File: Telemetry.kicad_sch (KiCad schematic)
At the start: 0 parts

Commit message: idk
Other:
- sheet LeaderSOM4 ports: added none; removed +12V_CarCAN, GND_CarCAN
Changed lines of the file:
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@@
 	(rectangle
 		(start 18.415 18.415)
-		(end 245.745 104.775)
+		(end 229.87 104.775)
 		(stroke
 			(width 0.508)
@@
 	)
 	(bus_entry
-		(at 38.735 60.96)
+		(at 38.1 60.96)
 		(size 2.54 -2.54)
 		(stroke
@@
 	)
 	(bus_entry
-		(at 38.735 57.15)
+		(at 38.1 57.15)
 		(size 2.54 -2.54)
 		(stroke
@@
 	)
 	(bus_entry
-		(at 38.735 53.34)
-		(size 2.54 -2.54)
-		(stroke
-			(width 0)
-			(type default)
-		)
-	)
-	(bus_entry
 		(at 153.035 34.29)
 		(size 2.54 2.54)
@@
 	)
 	(bus_entry
-		(at 38.735 64.77)
-		(size 2.54 -2.54)
-		(stroke
-			(width 0)
-			(type default)
-		)
-	)
-	(bus_entry
 		(at 206.375 30.48)
 		(size 2.54 2.54)
@@
 	(wire
 		(pts
+			(xy 40.64 58.42) (xy 41.91 58.42)
+		)
+		(stroke
+			(width 0)
+			(type default)
+		)
+	)
+	(wire
+		(pts
 			(xy 82.55 54.61) (xy 83.185 54.61)
 		)
@@
 	(bus
 		(pts
-			(xy 38.735 60.96) (xy 38.735 64.77)
-		)
-		(stroke
-			(width 0)
-			(type default)
-		)
-	)
-	(bus
-		(pts
 			(xy 85.725 57.15) (xy 85.725 60.96)
 		)
@@
 		)
 	)
-	(wire
-		(pts
-			(xy 41.275 54.61) (xy 41.91 54.61)
-		)
-		(stroke
-			(width 0)
-			(type default)
-		)
-	)
 	(bus
 		(pts
@@
 	(bus
 		(pts
-			(xy 38.735 57.15) (xy 38.735 60.96)
+			(xy 38.1 57.15) (xy 38.1 60.96)
 		)
 		(stroke
@@
 		(pts
 			(xy 108.585 52.705) (xy 121.285 52.705)
+		)
+		(stroke
+			(width 0)
+			(type default)
+		)
+	)
+	(wire
+		(pts
+			(xy 40.64 54.61) (xy 41.91 54.61)
 		)
 		(stroke
@@
 		)
 	)
+	(bus
+		(pts
+			(xy 38.1 60.96) (xy 38.1 62.23)
+		)
+		(stroke
+			(width 0)
+			(type default)
+		)
+	)
 	(wire
 		(pts
@@
 		(pts
 			(xy 82.55 50.8) (xy 83.185 50.8)
-		)
-		(stroke
-			(width 0)
-			(type default)
-		)
-	)
-	(wire
-		(pts
-			(xy 41.275 58.42) (xy 41.91 58.42)
 		)
 		(stroke
@@
 	(wire
 		(pts
-			(xy 41.275 50.8) (xy 41.91 50.8)
-		)
-		(stroke
-			(width 0)
-			(type default)
-		)
-	)
-	(bus
-		(pts
-			(xy 38.735 53.34) (xy 38.735 57.15)
-		)
-		(stroke
-			(width 0)
-			(type default)
-		)
-	)
-	(wire
-		(pts
-			(xy 41.275 62.23) (xy 41.91 62.23)
-		)
-		(stroke
-			(width 0)
-			(type default)
-		)
-	)
-	(wire
-		(pts
-			(xy 31.75 43.18) (xy 41.91 43.18)
+			(xy 35.56 43.18) (xy 41.91 43.18)
 		)
 		(stroke
@@
 		)
 	)
-	(bus
-		(pts
-			(xy 38.735 64.77) (xy 38.735 67.31)
-		)
-		(stroke
-			(width 0)
-			(type default)
-		)
-	)
 	(wire
 		(pts
@@
 	(wire
 		(pts
-			(xy 31.75 45.72) (xy 41.91 45.72)
+			(xy 35.56 45.72) (xy 41.91 45.72)
 		)
 		(stroke
@@
 		)
 	)
-	(label "12V_Out4"
-		(at 31.75 43.18 0)
-		(effects
-			(font
-				(size 1.27 1.27)
-			)
-			(justify left bottom)
-		)
-	)
 	(label "LTE"
 		(at 30.48 76.2 0)
@@
 	)
 	(label "CarCAN"
-		(at 38.735 61.595 180)
+		(at 38.1 60.96 180)
 		(effects
 			(font
@@
 		)
 	)
-	(label "GND_Out4"
-		(at 31.75 45.72 0)
-		(effects
-			(font
-				(size 1.27 1.27)
-			)
-			(justify left bottom)
-		)
-	)
 	(label "GPS"
 		(at 30.48 69.85 0)
@@
 			)
 			(justify left bottom)
+		)
+	)
+	(hierarchical_label "12V_In"
+		(shape input)
+		(at 35.56 43.18 180)
+		(effects
+			(font
+				(size 1.27 1.27)
+			)
+			(justify right)
+		)
+	)
+	(hierarchical_label "GND_In"
+		(shape input)
+		(at 35.56 45.72 180)
+		(effects
+			(font
+				(size 1.27 1.27)
+			)
+			(justify right)
 		)
 	)
@@
 			)
 		)
-		(pin "GND_CarCAN" input
-			(at 41.91 62.23 180)
-			(effects
-				(font
-					(size 1.27 1.27)
-				)
-				(justify left)
-			)
-		)
 		(pin "+12V_PCAN" output
 			(at 82.55 46.99 0)
@@
 			)
 		)
-		(pin "+12V_CarCAN" input
-			(at 41.91 50.8 180)
-			(effects
-				(font
-					(size 1.27 1.27)
-				)
-				(justify left)
-			)
-		)

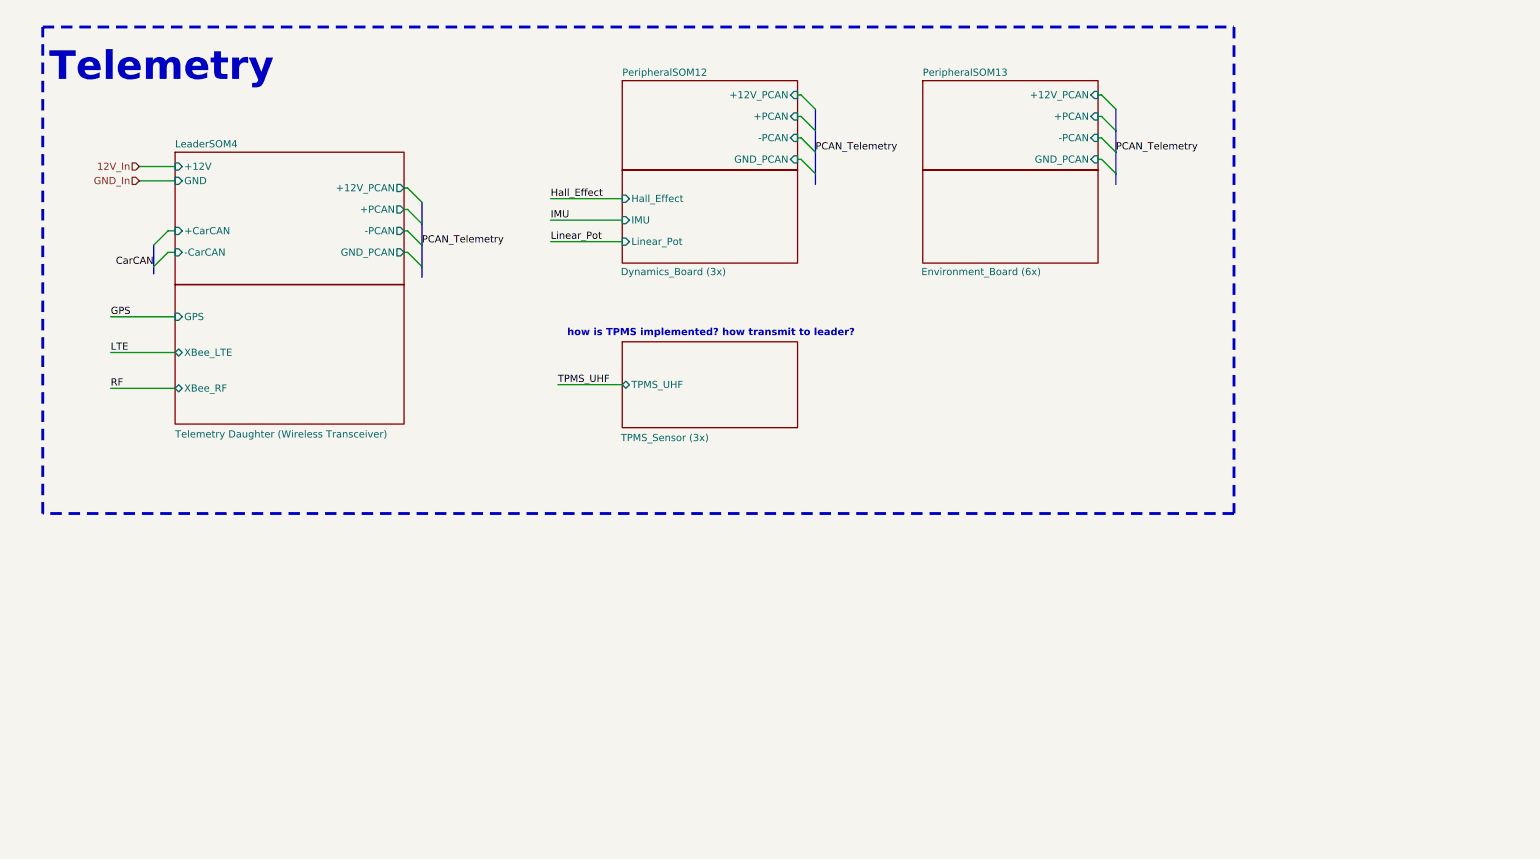
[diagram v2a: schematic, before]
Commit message: Updated Controls + Telemetry
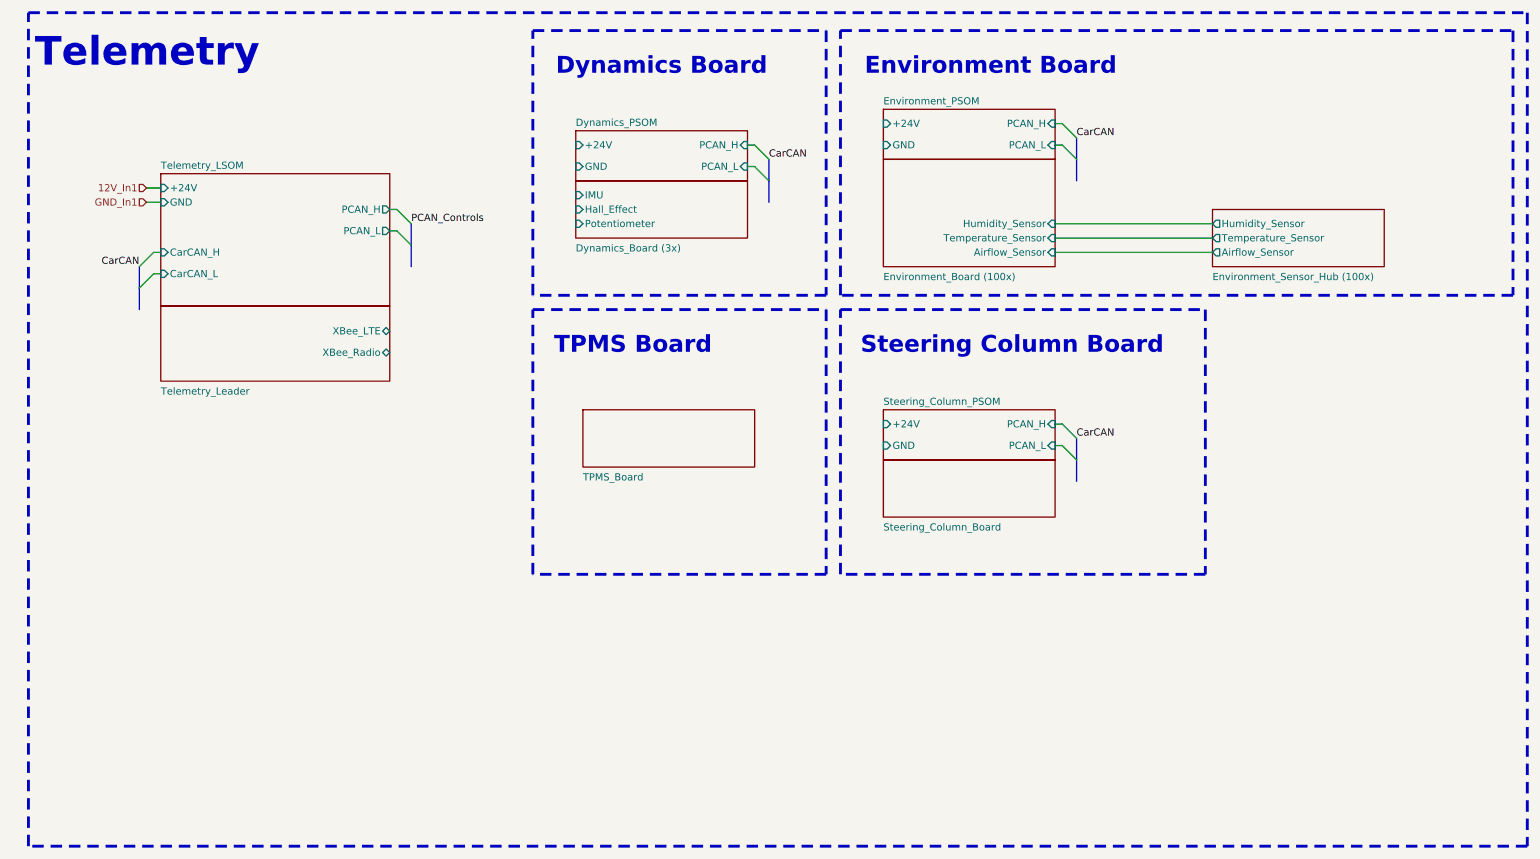
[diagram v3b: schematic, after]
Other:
- removed sheet Environment_Board (6x)
- removed sheet LeaderSOM4
- removed sheet PeripheralSOM12
- removed sheet PeripheralSOM13
- removed sheet TPMS_Sensor (3x)
- removed sheet Telemetry Daughter (Wireless Transceiver)
- added sheet Dynamics_PSOM (PeripheralSOM.kicad_sch)
- added sheet Environment_Board (100x) (Environment_Board.kicad_sch)
- added sheet Environment_PSOM (PeripheralSOM.kicad_sch)
- added sheet Environment_Sensor_Hub (100x) (Environment_Sensor_Hub.kicad_sch)
- added sheet Steering_Column_Board (Steering_Column_Board.kicad_sch)
- added sheet Steering_Column_PSOM (PeripheralSOM.kicad_sch)
- added sheet TPMS_Board (TPMS_Board.kicad_sch)
- added sheet Telemetry_LSOM (LeaderSOM.kicad_sch)
- added sheet Telemetry_Leader (Controls_Daugther.kicad_sch)
- sheet Dynamics_Board (3x) ports: added Potentiometer; removed Linear_Pot
- note added: "Dynamics Board"
- note added: "Environment Board"
- note added: "Steering Column Board"
- note added: "TPMS Board"
- note removed: "how is TPMS implemented? how transmit to leader?"
